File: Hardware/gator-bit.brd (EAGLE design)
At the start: 114.4 x 70.4 mm, 93 parts, among them J1 GATOR, J10 GATOR, J11 GATOR, J12 GATOR, J13 GATOR, J14 GATOR, J15 GATOR, J16 GATOR, J17 GATOR, J18 GATOR, J2 GATOR, J3 GATOR, J4 GATOR, J6 GATOR, J7 GATOR, J8 GATOR, J9 GATOR, U1 TPS63070, U2 micro:bit, U3 TXB0104, U4 ADJ REG 1.5A

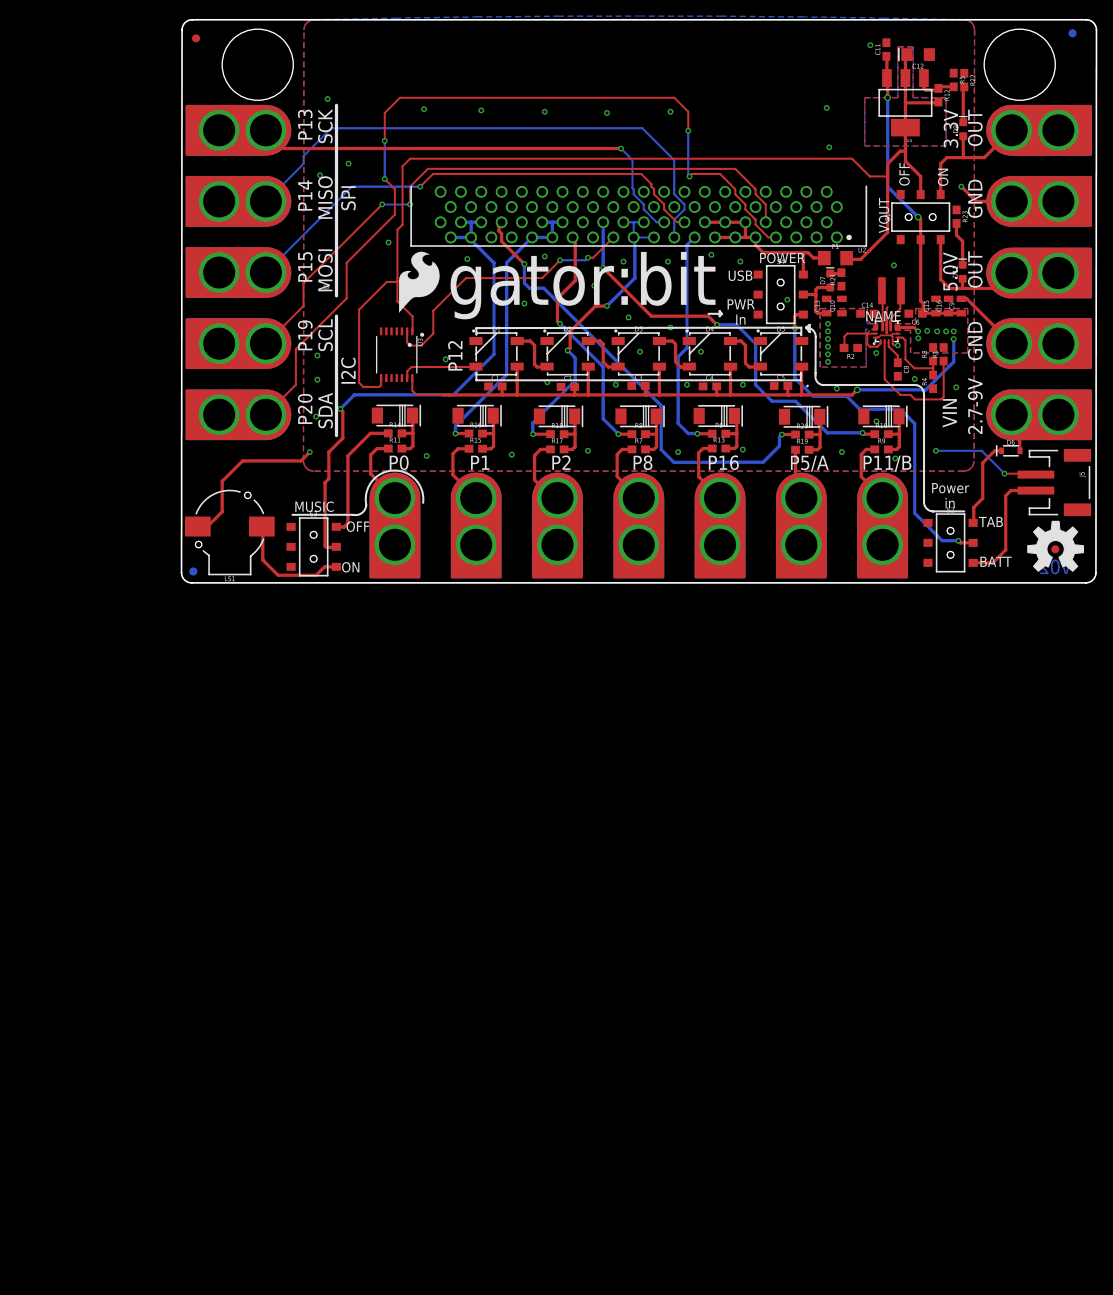
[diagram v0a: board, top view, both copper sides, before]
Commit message: added logos
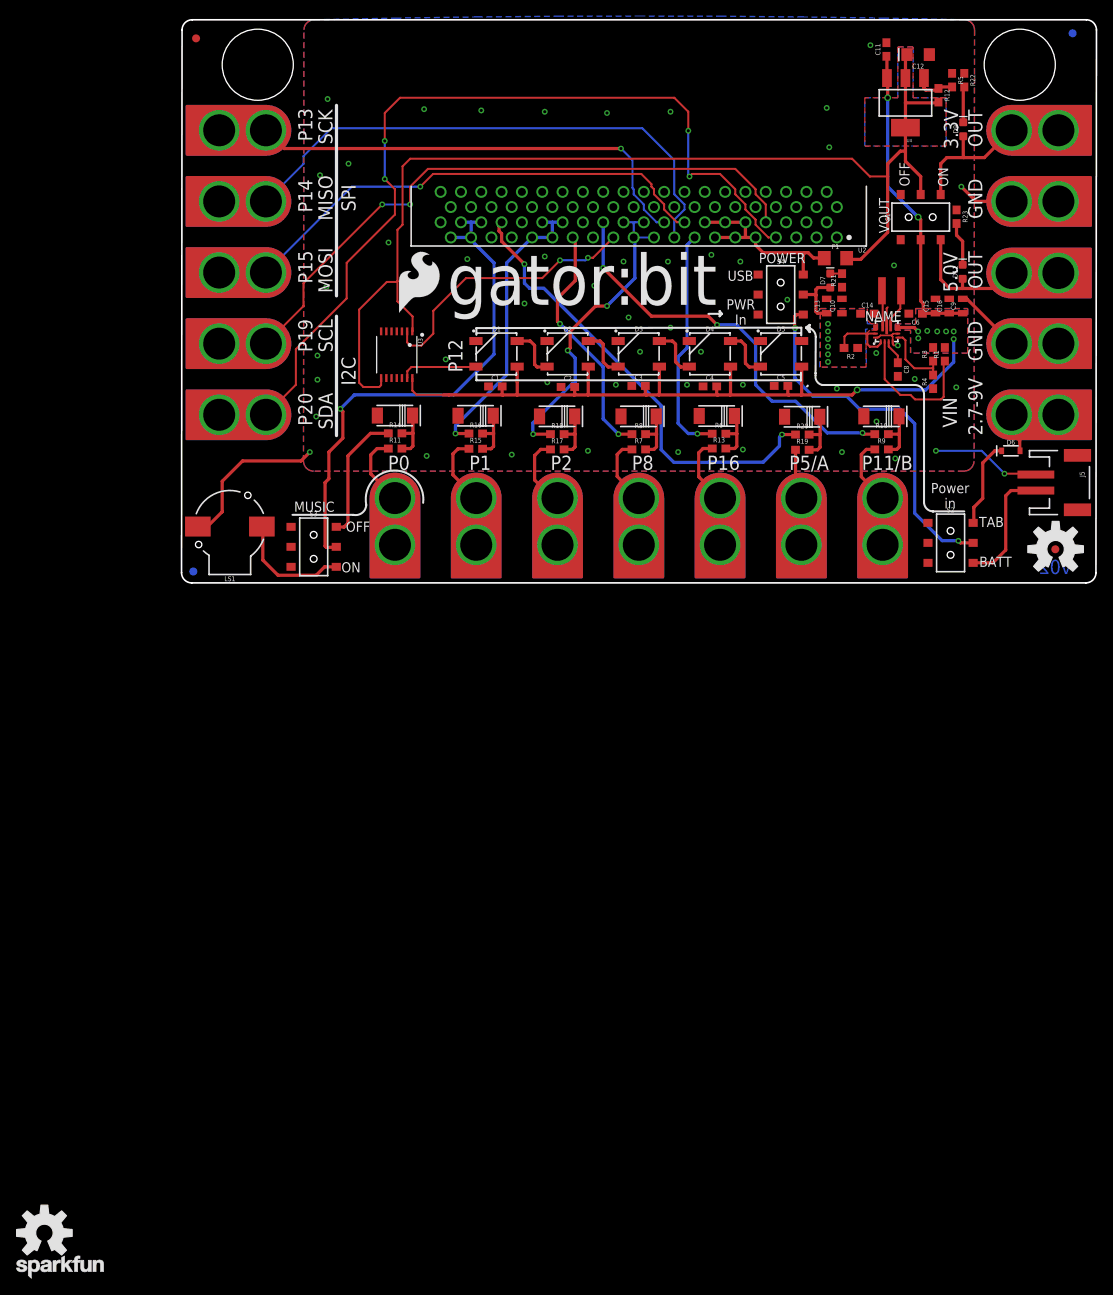
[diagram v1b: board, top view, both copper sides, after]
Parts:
- added LOGO1: OSHW-LOGOL, SparkFun-Aesthetics:OSHW-LOGO-L
- added LOGO2: SFE_LOGO_NAME.1_INCH, SparkFun-Aesthetics:SFE_LOGO_NAME_.1
- moved R5 0.20 mm to (96.3, 62.8)
- moved C9 0.18 mm to (97.7, 34.6)
- moved R1 0.15 mm to (95.4, 28.6)
- moved R21 0.15 mm to (82.6, 37.8)
- moved C16 0.08 mm to (96.0, 34.6)
- moved C15 0.05 mm to (94.2, 34.6)
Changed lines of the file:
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@@
 <layer number="19" name="Unrouted" color="6" fill="1" visible="yes" active="yes"/>
 <layer number="20" name="Dimension" color="15" fill="1" visible="yes" active="yes"/>
-<layer number="21" name="tPlace" color="16" fill="1" visible="yes" active="yes"/>
+<layer number="21" name="tPlace" color="16" fill="1" visible="no" active="yes"/>
 <layer number="22" name="bPlace" color="14" fill="1" visible="no" active="yes"/>
 <layer number="23" name="tOrigins" color="15" fill="1" visible="yes" active="yes"/>
@@
 <layer number="27" name="tValues" color="7" fill="1" visible="no" active="yes"/>
 <layer number="28" name="bValues" color="7" fill="1" visible="no" active="yes"/>
-<layer number="29" name="tStop" color="7" fill="3" visible="no" active="yes"/>
-<layer number="30" name="bStop" color="7" fill="6" visible="no" active="yes"/>
-<layer number="31" name="tCream" color="7" fill="4" visible="no" active="yes"/>
-<layer number="32" name="bCream" color="7" fill="5" visible="no" active="yes"/>
-<layer number="39" name="tKeepout" color="4" fill="11" visible="no" active="yes"/>
-<layer number="40" name="bKeepout" color="1" fill="11" visible="no" active="yes"/>
-<layer number="41" name="tRestrict" color="4" fill="10" visible="no" active="yes"/>
-<layer number="42" name="bRestrict" color="1" fill="10" visible="no" active="yes"/>
+<layer number="29" name="tStop" color="7" fill="3" visible="yes" active="yes"/>
+<layer number="30" name="bStop" color="7" fill="6" visible="yes" active="yes"/>
+<layer number="31" name="tCream" color="7" fill="4" visible="yes" active="yes"/>
+<layer number="32" name="bCream" color="7" fill="5" visible="yes" active="yes"/>
+<layer number="39" name="tKeepout" color="4" fill="11" visible="yes" active="yes"/>
+<layer number="40" name="bKeepout" color="1" fill="11" visible="yes" active="yes"/>
+<layer number="41" name="tRestrict" color="4" fill="10" visible="yes" active="yes"/>
+<layer number="42" name="bRestrict" color="1" fill="10" visible="yes" active="yes"/>
 <layer number="43" name="vRestrict" color="2" fill="10" visible="no" active="yes"/>
 <layer number="44" name="Drills" color="7" fill="1" visible="no" active="yes"/>
@@
 <layer number="46" name="Milling" color="3" fill="1" visible="no" active="yes"/>
 <layer number="47" name="Measures" color="7" fill="1" visible="no" active="yes"/>
-<layer number="51" name="tDocu" color="6" fill="1" visible="yes" active="yes"/>
+<layer number="51" name="tDocu" color="6" fill="1" visible="no" active="yes"/>
 <layer number="52" name="bDocu" color="7" fill="1" visible="no" active="yes"/>
 <layer number="3" name="Route3" color="4" fill="3" visible="no" active="no"/>
@@
 <attribute name="PROD_ID" value="IC-13858" x="89.535" y="30.1625" size="1.778" layer="27" rot="R90" display="off"/>
 </element>
-<element name="R1" library="SparkFun-Resistors" package="0603" value="100k" x="95.2627" y="28.575" rot="R90">
-<attribute name="PROD_ID" value="RES-07828" x="95.2627" y="28.575" size="1.778" layer="27" rot="R90" display="off"/>
+<element name="R1" library="SparkFun-Resistors" package="0603" value="100k" x="95.4151" y="28.575" rot="R90">
+<attribute name="PROD_ID" value="RES-07828" x="95.4151" y="28.575" size="1.778" layer="27" rot="R90" display="off"/>
 </element>
 <element name="R2" library="SparkFun-Resistors" package="0603" value="10.2K" x="83.66125" y="29.36875" rot="R180">
@@
 <attribute name="PROD_ID" value="VREG-12029" x="90.4875" y="60.0075" size="1.778" layer="27" rot="R180" display="off"/>
 </element>
-<element name="R5" library="SparkFun-Resistors" package="0603" value="390k" x="96.52" y="62.865" rot="R270">
-<attribute name="PROD_ID" value="RES-12024" x="96.52" y="62.865" size="1.778" layer="27" rot="R270" display="off"/>
+<element name="R5" library="SparkFun-Resistors" package="0603" value="390k" x="96.3168" y="62.8396" rot="R270">
+<attribute name="PROD_ID" value="RES-12024" x="96.3168" y="62.8396" size="1.778" layer="27" rot="R270" display="off"/>
 </element>
 <element name="R12" library="SparkFun-Resistors" package="0603" value="240" x="94.615" y="60.96" rot="R270">
@@
 <attribute name="PROD_ID" value="CAP-11015" x="85.725" y="33.655" size="1.778" layer="27" display="off"/>
 </element>
-<element name="C9" library="SparkFun-Capacitors" package="0805" value="22uF" x="97.4725" y="34.6075" rot="R90">
-<attribute name="PROD_ID" value="CAP-08402" x="97.4725" y="34.6075" size="1.778" layer="27" rot="R90" display="off"/>
-</element>
-<element name="C15" library="SparkFun-Capacitors" package="0805" value="22uF" x="94.2975" y="34.6075" rot="R90">
-<attribute name="PROD_ID" value="CAP-08402" x="94.2975" y="34.6075" size="1.778" layer="27" rot="R90" display="off"/>
-</element>
-<element name="C16" library="SparkFun-Capacitors" package="0805" value="22uF" x="95.885" y="34.6075" rot="R90">
-<attribute name="PROD_ID" value="CAP-08402" x="95.885" y="34.6075" size="1.778" layer="27" rot="R90" display="off"/>
+<element name="C9" library="SparkFun-Capacitors" package="0805" value="22uF" x="97.6503" y="34.6075" rot="R90">
+<attribute name="PROD_ID" value="CAP-08402" x="97.6503" y="34.6075" size="1.778" layer="27" rot="R90" display="off"/>
+</element>
+<element name="C15" library="SparkFun-Capacitors" package="0805" value="22uF" x="94.2467" y="34.6075" rot="R90">
+<attribute name="PROD_ID" value="CAP-08402" x="94.2467" y="34.6075" size="1.778" layer="27" rot="R90" display="off"/>
+</element>
+<element name="C16" library="SparkFun-Capacitors" package="0805" value="22uF" x="95.9612" y="34.6075" rot="R90">
+<attribute name="PROD_ID" value="CAP-08402" x="95.9612" y="34.6075" size="1.778" layer="27" rot="R90" display="off"/>
 </element>
 <element name="U3" library="SparkFun-IC-Comms" package="TSSOP14" value="TXB0104" x="26.8986" y="28.5242" rot="R180">
@@
 <attribute name="SF_ID" value="COM-00597" x="74.8919" y="36.0426" size="1.778" layer="27" rot="R270" display="off"/>
 </element>
-<element name="R21" library="SparkFun-Resistors" package="0603" value="1k" x="82.4865" y="37.9349" rot="R90">
-<attribute name="PROD_ID" value="RES-07856" x="82.4865" y="37.9349" size="1.778" layer="27" rot="R90" display="off"/>
+<element name="R21" library="SparkFun-Resistors" package="0603" value="1k" x="82.5627" y="37.8079" rot="R90">
+<attribute name="PROD_ID" value="RES-07856" x="82.5627" y="37.8079" size="1.778" layer="27" rot="R90" display="off"/>
 </element>
 <element name="R22" library="SparkFun-Resistors" package="0603" value="1k" x="97.8408" y="62.8396" rot="R270">
@@
 <attribute name="PROD_ID" value="RES-08585" x="81.7372" y="40.5892" size="1.778" layer="27" display="off"/>
 </element>
+<element name="LOGO1" library="SparkFun-Aesthetics" package="OSHW-LOGO-L" value="OSHW-LOGOL" x="-17.145" y="-81.2546"/>
+<element name="LOGO2" library="SparkFun-Aesthetics" package="SFE_LOGO_NAME_.1" value="SFE_LOGO_NAME.1_INCH" x="-21.1328" y="-87.4268"/>
 </elements>
 <signals>
@@
 <via x="45.72" y="25.0825" extent="1-16" drill="0.381"/>
 <via x="33.02" y="27.94" extent="1-16" drill="0.381"/>
-<wire x1="97.4725" y1="35.5075" x2="98.1615" y2="35.5075" width="0.4064" layer="1"/>
+<wire x1="97.6503" y1="35.5075" x2="98.1615" y2="35.5075" width="0.4064" layer="1"/>
 <wire x1="98.1615" y1="35.5075" x2="103.764" y2="29.905" width="0.4064" layer="1"/>
 <contactref element="R21" pad="1"/>
@@
 <wire x1="89.8525" y1="23.495" x2="91.1225" y2="23.495" width="0.254" layer="1"/>
 <wire x1="91.1225" y1="23.495" x2="91.6813" y2="22.9362" width="0.254" layer="1"/>
-<wire x1="95.2627" y1="27.725" x2="95.2627" y2="23.2537" width="0.254" layer="1"/>
 <wire x1="95.2627" y1="23.2537" x2="94.9452" y2="22.9362" width="0.254" layer="1"/>
 <wire x1="94.9452" y1="22.9362" x2="91.6813" y2="22.9362" width="0.254" layer="1"/>
+<wire x1="95.2627" y1="23.2537" x2="95.2627" y2="27.5726" width="0.254" layer="1"/>
+<wire x1="95.2627" y1="27.5726" x2="95.4151" y2="27.725" width="0.254" layer="1"/>
 </signal>
 <signal name="5V">
@@
 <wire x1="77.512" y1="27.035" x2="77.512" y2="23.537" width="0.4064" layer="1"/>
 <wire x1="77.512" y1="23.537" x2="77.47" y2="23.495" width="0.4064" layer="1"/>
-<wire x1="97.4725" y1="33.7075" x2="95.885" y2="33.7075" width="0.4064" layer="1"/>
-<wire x1="95.885" y1="33.7075" x2="94.2975" y2="33.7075" width="0.4064" layer="1"/>
-<wire x1="94.2975" y1="33.7075" x2="92.66" y2="33.7075" width="0.4064" layer="1"/>
+<wire x1="97.6503" y1="33.7075" x2="95.9612" y2="33.7075" width="0.4064" layer="1"/>
+<wire x1="95.9612" y1="33.7075" x2="94.2467" y2="33.7075" width="0.4064" layer="1"/>
+<wire x1="94.2467" y1="33.7075" x2="92.66" y2="33.7075" width="0.4064" layer="1"/>
 <wire x1="92.66" y1="33.7075" x2="92.6075" y2="33.655" width="0.4064" layer="1"/>
 <wire x1="89.529" y1="31.9196625" x2="91.5878375" y2="31.9196625" width="0.4064" layer="1"/>
@@
 <wire x1="93.0275" y1="61.595" x2="94.4" y2="61.595" width="0.4064" layer="1"/>
 <wire x1="94.4" y1="61.595" x2="94.615" y2="61.81" width="0.4064" layer="1"/>
-<wire x1="96.52" y1="62.015" x2="94.82" y2="62.015" width="0.4064" layer="1"/>
-<wire x1="94.82" y1="62.015" x2="94.615" y2="61.81" width="0.4064" layer="1"/>
+<wire x1="96.3168" y1="61.9896" x2="94.7946" y2="61.9896" width="0.4064" layer="1"/>
+<wire x1="94.7946" y1="61.9896" x2="94.615" y2="61.81" width="0.4064" layer="1"/>
 </signal>
 <signal name="N$17">
@@
 <contactref element="D7" pad="C"/>
 <contactref element="R21" pad="2"/>
-<wire x1="81.0895" y1="38.6722" x2="82.3738" y2="38.6722" width="0.4064" layer="1"/>
-<wire x1="82.3738" y1="38.6722" x2="82.4865" y2="38.7849" width="0.4064" layer="1"/>
+<wire x1="81.0895" y1="38.6722" x2="82.5484" y2="38.6722" width="0.254" layer="1"/>
+<wire x1="82.5484" y1="38.6722" x2="82.5627" y2="38.6579" width="0.254" layer="1"/>
 </signal>
 <signal name="N$23">
